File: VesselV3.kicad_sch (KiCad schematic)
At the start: 396 parts, among them IC1 USB3320C-EZK-TR, IC3 5VOutput_VoltageRegulator, IC4 BidirectionalLogicLevelShifter, IC6 AND Gate, J1 JTAG/SWD 10pins Headers, Y1 25MHz

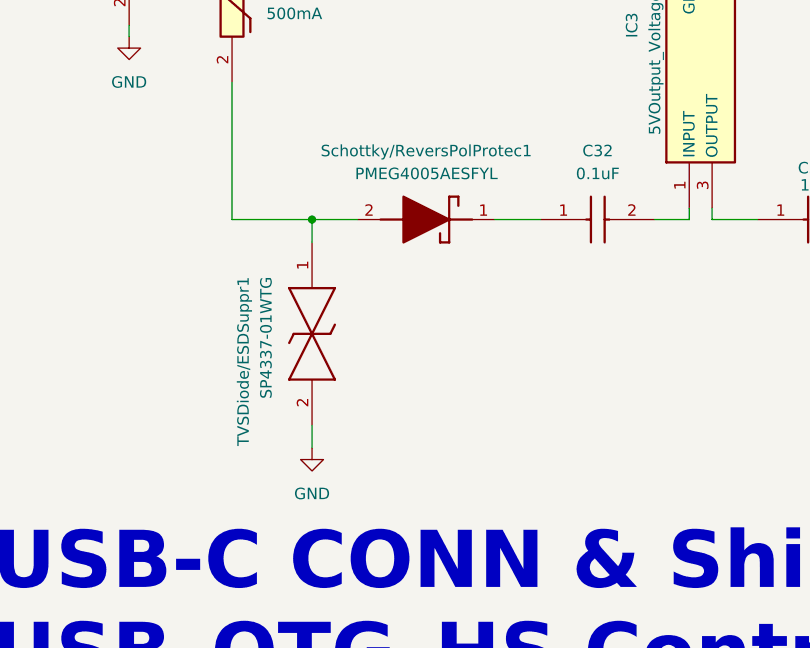
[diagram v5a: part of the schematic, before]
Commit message: Fixed DRC Errors
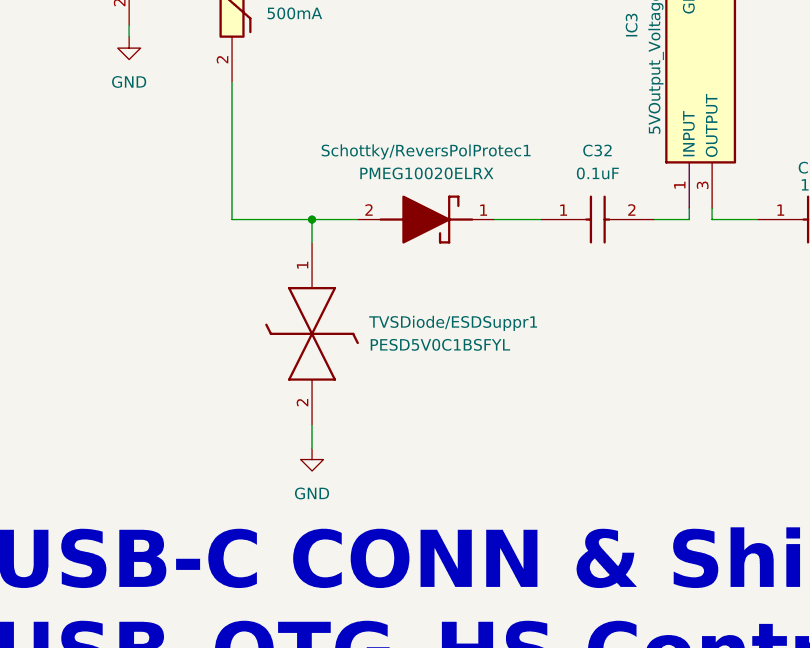
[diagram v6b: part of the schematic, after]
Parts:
- removed Schottky/ReversPolProtec1: PMEG4005AESFYL, SamacSys_Parts:PMEG4005AESFYL, symbol SamacSys_Parts:PMEG4005AESFYL
- removed TVSDiode/ESDSuppr1: SP4337-01WTG, SamacSys_Parts:SP433701WTG, symbol SamacSys_Parts:SP4337-01WTG
- added Schottky/ReversPolProtec1: PMEG10020ELRX, SODFL3517X110N, symbol SamacSys_Parts:PMEG10020ELRX
- added TVSDiode/ESDSuppr1: PESD5V0C1BSFYL, PMEG3005AESFYL, symbol SamacSys_Parts:PESD5V0C1BSFYL
- H1, H2, H3, H4: footprint MountingHole:MountingHole_2.5mm_Pad_Via -> MountingHole:MountingHole_2.5mm_Pad_TopBottom
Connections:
- net GND: now also TVSDiode/ESDSuppr1.2 (K2)
- net at C32.1: now also Schottky/ReversPolProtec1.1 (K)
- net at Polyfuse1.2: now also Schottky/ReversPolProtec1.2 (A), TVSDiode/ESDSuppr1.1 (K1)
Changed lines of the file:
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@@
     )
   )
+  (symbol (lib_id "SamacSys_Parts:PMEG10020ELRX") (at 306.07 81.28 180) (unit 1)
+    (in_bom yes) (on_board yes) (dnp no) (fields_autoplaced)
+    (property "Reference" "Schottky/ReversPolProtec1" (at 295.91 73.66 0)
+      (effects (font (size 1.27 1.27)))
+    )
+    (property "Value" "PMEG10020ELRX" (at 295.91 76.2 0)
+      (effects (font (size 1.27 1.27)))
+    )
+    (property "Footprint" "SODFL3517X110N" (at 293.37 -12.37 0)
+      (effects (font (size 1.27 1.27)) (justify left top) hide)
+    )
+    (property "Datasheet" "https://assets.nexperia.com/documents/data-sheet/PMEG10020ELR.pdf" (at 293.37 -112.37 0)
+      (effects (font (size 1.27 1.27)) (justify left top) hide)
+    )
+    (property "Height" "1.1" (at 293.37 -312.37 0)
+      (effects (font (size 1.27 1.27)) (justify left top) hide)
+    )
+    (property "Mouser Part Number" "771-PMEG10020ELRX" (at 293.37 -412.37 0)
+      (effects (font (size 1.27 1.27)) (justify left top) hide)
+    )
+    (property "Mouser Price/Stock" "https://www.mouser.co.uk/ProductDetail/Nexperia/PMEG10020ELRX?qs=bel5lzaZNxQmrosujSY5VA%3D%3D" (at 293.37 -512.37 0)
+      (effects (font (size 1.27 1.27)) (justify left top) hide)
+    )
+    (property "Manufacturer_Name" "Nexperia" (at 293.37 -612.37 0)
+      (effects (font (size 1.27 1.27)) (justify left top) hide)
+    )
+    (property "Manufacturer_Part_Number" "PMEG10020ELRX" (at 293.37 -712.37 0)
+      (effects (font (size 1.27 1.27)) (justify left top) hide)
+    )
+    (property "DigikeyPartNumber" "1727-2396-2-ND" (at 306.07 81.28 0)
+      (effects (font (size 1.27 1.27)) hide)
+    )
+    (pin "1")
+    (pin "2")
+    (instances
+      (project "VesselV3"
+        (path "/7364f6a3-b999-47c8-8f6d-f83e5421d1ed"
+          (reference "Schottky/ReversPolProtec1") (unit 1)
+        )
+      )
+    )
+  )
   (symbol (lib_id "WS2812BNano4684RGB-3rdParty:4684") (at 454.66 419.1 0) (mirror y) (unit 1)
     (in_bom yes) (on_board yes) (dnp no)
@@
       (effects (font (size 1.27 1.27)) (justify left))
     )
-    (property "Footprint" "MountingHole:MountingHole_2.5mm_Pad_Via" (at 445.77 201.93 0)
+    (property "Footprint" "MountingHole:MountingHole_2.5mm_Pad_TopBottom" (at 445.77 201.93 0)
       (effects (font (size 1.27 1.27)) hide)
     )
@@
     )
   )
+  (symbol (lib_id "SamacSys_Parts:PESD5V0C1BSFYL") (at 283.21 83.82 270) (unit 1)
+    (in_bom yes) (on_board yes) (dnp no)
+    (property "Reference" "TVSDiode/ESDSuppr1" (at 289.56 92.71 90)
+      (effects (font (size 1.27 1.27)) (justify left))
+    )
+    (property "Value" "PESD5V0C1BSFYL" (at 289.56 95.25 90)
+      (effects (font (size 1.27 1.27)) (justify left))
+    )
+    (property "Footprint" "PMEG3005AESFYL" (at 189.56 99.06 0)
+      (effects (font (size 1.27 1.27)) (justify left bottom) hide)
+    )
+    (property "Datasheet" "https://assets.nexperia.com/documents/data-sheet/PESD5V0C1BSF.pdf" (at 89.56 99.06 0)
+      (effects (font (size 1.27 1.27)) (justify left bottom) hide)
+    )
+    (property "Height" "" (at -110.44 99.06 0)
+      (effects (font (size 1.27 1.27)) (justify left bottom) hide)
+    )
+    (property "Mouser Part Number" "771-PESD5V0C1BSFYL" (at -210.44 99.06 0)
+      (effects (font (size 1.27 1.27)) (justify left bottom) hide)
+    )
+    (property "Mouser Price/Stock" "https://www.mouser.co.uk/ProductDetail/Nexperia/PESD5V0C1BSFYL?qs=Pve5fMu%2FDEv%252BAQF4BlT7Aw%3D%3D" (at -310.44 99.06 0)
+      (effects (font (size 1.27 1.27)) (justify left bottom) hide)
+    )
+    (property "Manufacturer_Name" "Nexperia" (at -410.44 99.06 0)
+      (effects (font (size 1.27 1.27)) (justify left bottom) hide)
+    )
+    (property "Manufacturer_Part_Number" "PESD5V0C1BSFYL" (at -510.44 99.06 0)
+      (effects (font (size 1.27 1.27)) (justify left bottom) hide)
+    )
+    (property "DigikeyPartNumber" "ESD9B5.0ST5GOSTR-ND" (at 283.21 83.82 0)
+      (effects (font (size 1.27 1.27)) hide)
+    )
+    (pin "1")
+    (pin "2")
+    (instances
+      (project "VesselV3"
+        (path "/7364f6a3-b999-47c8-8f6d-f83e5421d1ed"
+          (reference "TVSDiode/ESDSuppr1") (unit 1)
+        )
+      )
+    )
+  )
   (symbol (lib_id "SamacSys_Parts:0402ZC103JAT2A") (at 633.73 257.81 270) (unit 1)
     (in_bom yes) (on_board yes) (dnp no) (fields_autoplaced)
@@
     )
   )
-  (symbol (lib_id "SamacSys_Parts:PMEG4005AESFYL") (at 306.07 81.28 180) (unit 1)
-    (in_bom yes) (on_board yes) (dnp no) (fields_autoplaced)
-    (property "Reference" "Schottky/ReversPolProtec1" (at 295.91 73.66 0)
-      (effects (font (size 1.27 1.27)))
-    )
-    (property "Value" "PMEG4005AESFYL" (at 295.91 76.2 0)
-      (effects (font (size 1.27 1.27)))
-    )
-    (property "Footprint" "SamacSys_Parts:PMEG4005AESFYL" (at 293.37 -12.37 0)
-      (effects (font (size 1.27 1.27)) (justify left top) hide)
-    )
-    (property "Datasheet" "https://assets.nexperia.com/documents/data-sheet/PMEG4005AESF.pdf" (at 293.37 -112.37 0)
-      (effects (font (size 1.27 1.27)) (justify left top) hide)
-    )
-    (property "Height" "0.32" (at 293.37 -312.37 0)
-      (effects (font (size 1.27 1.27)) (justify left top) hide)
-    )
-    (property "Mouser Part Number" "771-PMEG4005AESFYL" (at 293.37 -412.37 0)
-      (effects (font (size 1.27 1.27)) (justify left top) hide)
-    )
-    (property "Mouser Price/Stock" "https://www.mouser.co.uk/ProductDetail/Nexperia/PMEG4005AESFYL?qs=Yna0arPQ0CT21It55ddDRA%3D%3D" (at 293.37 -512.37 0)
-      (effects (font (size 1.27 1.27)) (justify left top) hide)
-    )
-    (property "Manufacturer_Name" "Nexperia" (at 293.37 -612.37 0)
-      (effects (font (size 1.27 1.27)) (justify left top) hide)
-    )
-    (property "Manufacturer_Part_Number" "PMEG4005AESFYL" (at 293.37 -712.37 0)
-      (effects (font (size 1.27 1.27)) (justify left top) hide)
-    )
-    (property "DigikeyPartNumber" "1727-2295-2-ND" (at 306.07 81.28 0)
-      (effects (font (size 1.27 1.27)) hide)
-    )
-    (pin "1")
-    (pin "2")
-    (instances
-      (project "VesselV3"
-        (path "/7364f6a3-b999-47c8-8f6d-f83e5421d1ed"
-          (reference "Schottky/ReversPolProtec1") (unit 1)
-        )
-      )
-    )
-  )
   (symbol (lib_id "PCM_marbastlib-mx:MX_SW_solder") (at 180.34 154.94 0) (unit 1)
     (in_bom yes) (on_board yes) (dnp no) (fields_autoplaced)
@@
     )
   )
-  (symbol (lib_id "SamacSys_Parts:SP4337-01WTG") (at 283.21 83.82 270) (unit 1)
-    (in_bom yes) (on_board yes) (dnp no)
-    (property "Reference" "TVSDiode/ESDSuppr1" (at 275.59 87.63 0)
-      (effects (font (size 1.27 1.27)) (justify left))
-    )
-    (property "Value" "SP4337-01WTG" (at 278.13 87.63 0)
-      (effects (font (size 1.27 1.27)) (justify left))
-    )
-    (property "Footprint" "SamacSys_Parts:SP433701WTG" (at 189.56 96.52 0)
-      (effects (font (size 1.27 1.27)) (justify left bottom) hide)
-    )
-    (property "Datasheet" "https://www.littelfuse.com/media?resourcetype=datasheets&itemid=05af24f9-10ca-45b2-ba87-1809e744c005&filename=littelfuse-tvs-diode-array-sp4337-datasheet" (at 89.56 96.52 0)
-      (effects (font (size 1.27 1.27)) (justify left bottom) hide)
-    )
-    (property "Height" "0.329" (at -110.44 96.52 0)
-      (effects (font (size 1.27 1.27)) (justify left bottom) hide)
-    )
-    (property "Mouser Part Number" "576-SP4337-01WTG" (at -210.44 96.52 0)
-      (effects (font (size 1.27 1.27)) (justify left bottom) hide)
-    )
-    (property "Mouser Price/Stock" "https://www.mouser.co.uk/ProductDetail/Littelfuse/SP4337-01WTG?qs=pUKx8fyJudAYJw%2FQBO13Pg%3D%3D" (at -310.44 96.52 0)
-      (effects (font (size 1.27 1.27)) (justify left bottom) hide)
-    )
-    (property "Manufacturer_Name" "LITTELFUSE" (at -410.44 96.52 0)
-      (effects (font (size 1.27 1.27)) (justify left bottom) hide)
-    )
-    (property "Manufacturer_Part_Number" "SP4337-01WTG" (at -510.44 96.52 0)
-      (effects (font (size 1.27 1.27)) (justify left bottom) hide)
-    )
-    (property "DigikeyPartNumber" "18-SP4337-01WTGTR-ND" (at 283.21 83.82 0)
-      (effects (font (size 1.27 1.27)) hide)
-    )
-    (pin "1")
-    (pin "2")
-    (instances
-      (project "VesselV3"
-        (path "/7364f6a3-b999-47c8-8f6d-f83e5421d1ed"
-          (reference "TVSDiode/ESDSuppr1") (unit 1)
-        )
-      )
-    )
-  )
   (symbol (lib_id "PCM_marbastlib-mx:MX_SW_solder") (at 60.96 71.12 0) (unit 1)
     (in_bom yes) (on_board yes) (dnp no) (fields_autoplaced)
@@
       (effects (font (size 1.27 1.27)) (justify left))
     )
-    (property "Footprint" "MountingHole:MountingHole_2.5mm_Pad_Via" (at 445.77 194.31 0)
+    (property "Footprint" "MountingHole:MountingHole_2.5mm_Pad_TopBottom" (at 445.77 194.31 0)
       (effects (font (size 1.27 1.27)) hide)
     )
@@
       (effects (font (size 1.27 1.27)) (justify left))
     )
-    (property "Footprint" "MountingHole:MountingHole_2.5mm_Pad_Via" (at 426.72 201.93 0)
+    (property "Footprint" "MountingHole:MountingHole_2.5mm_Pad_TopBottom" (at 426.72 201.93 0)
       (effects (font (size 1.27 1.27)) hide)
     )
@@
       (effects (font (size 1.27 1.27)) (justify left))
     )
-    (property "Footprint" "MountingHole:MountingHole_2.5mm_Pad_Via" (at 426.72 194.31 0)
+    (property "Footprint" "MountingHole:MountingHole_2.5mm_Pad_TopBottom" (at 426.72 194.31 0)
       (effects (font (size 1.27 1.27)) hide)
     )

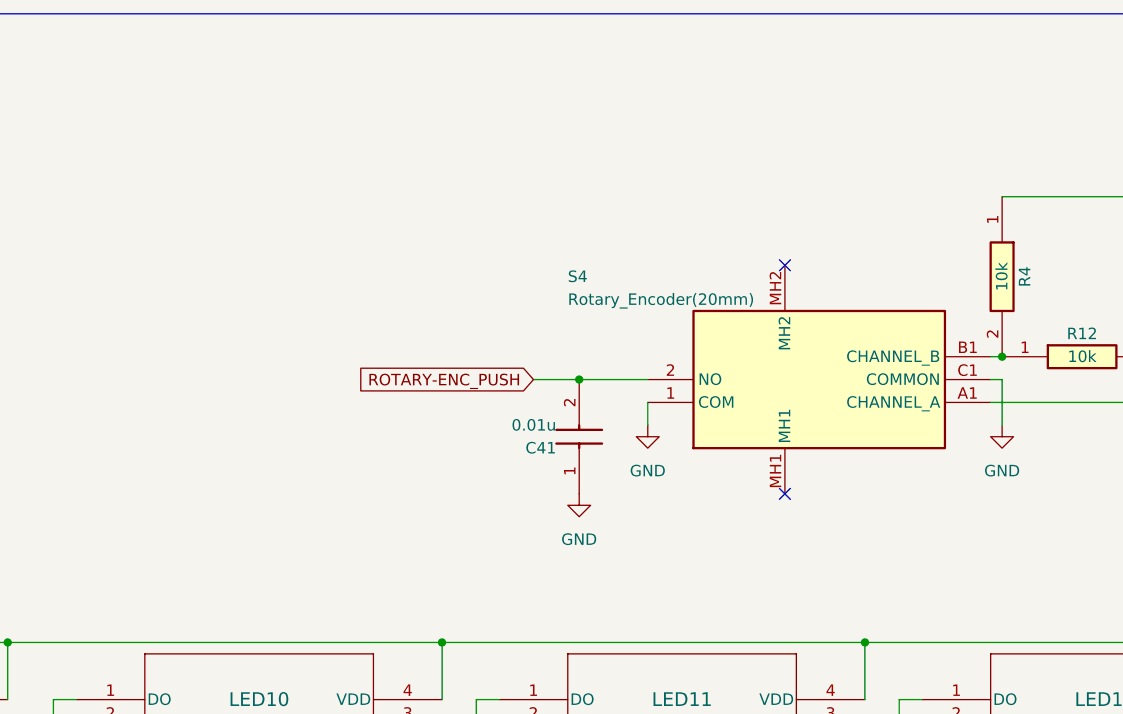
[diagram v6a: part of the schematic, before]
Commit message: Encoder Push - Pull-up and DRC
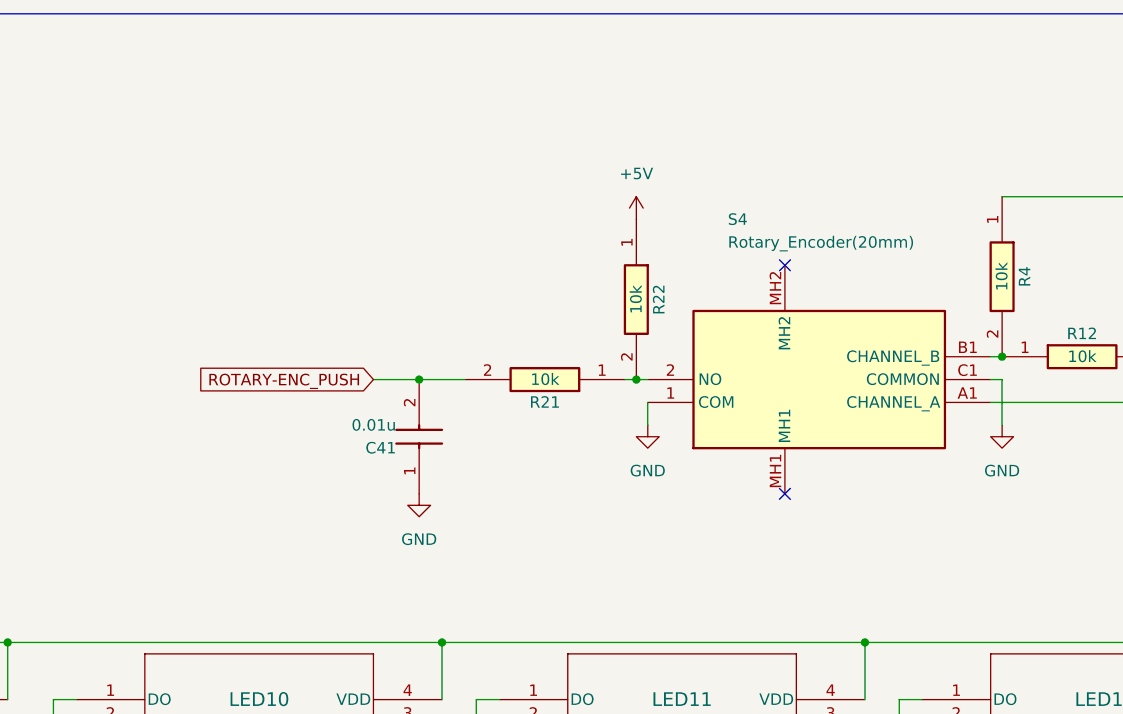
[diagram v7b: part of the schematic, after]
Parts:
- added R21, R22: 10k, SamacSys_Parts:RESC2012X50N, symbol SamacSys_Parts:CRCW080510K0JNEC
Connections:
- net +5V: now also R22.1
- net ROTARY-ENC_PUSH: now also R21.2; no longer S4.2 (NO)
- new net: R21.1, R22.2, S4.2 (NO)
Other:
- moved on the sheet: C41
